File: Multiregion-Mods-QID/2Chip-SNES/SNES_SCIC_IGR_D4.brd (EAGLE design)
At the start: 88.9 x 37.5 mm, 27 parts, among them IC1 74HC27D, IC2 74HC30D

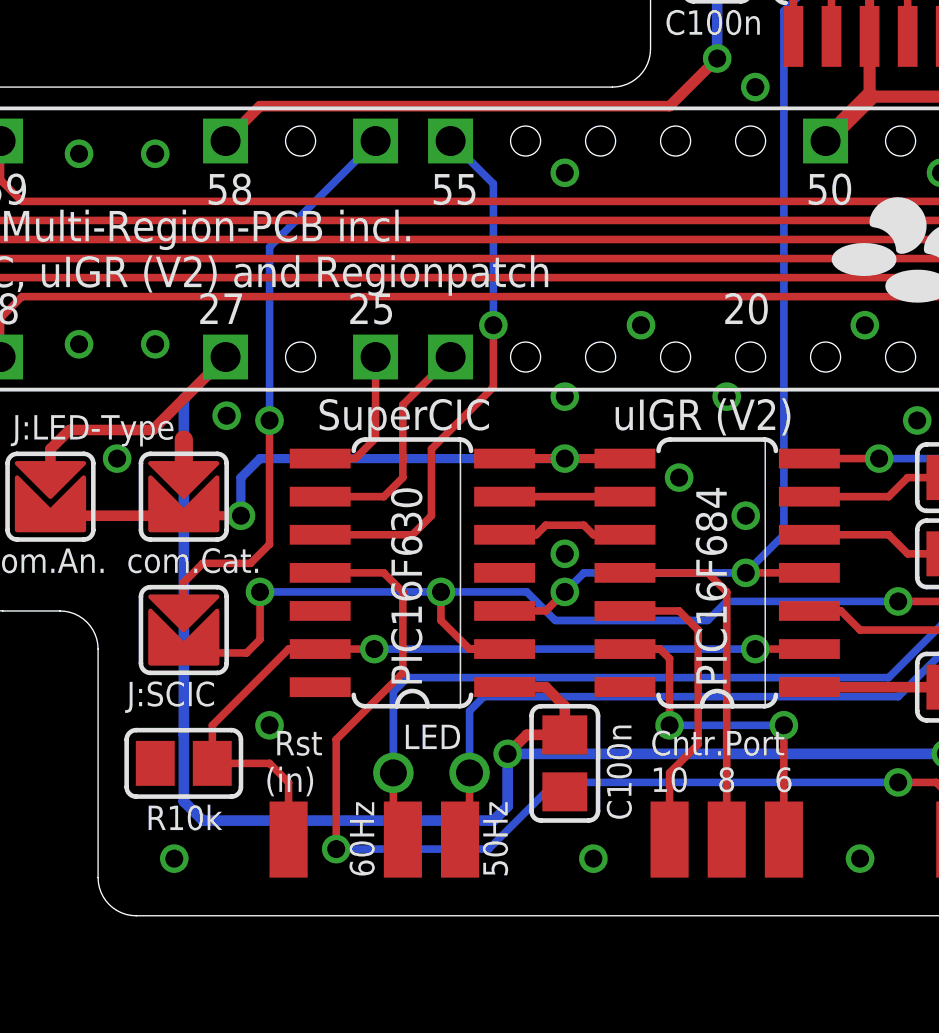
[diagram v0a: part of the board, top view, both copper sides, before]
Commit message: Minor Update (routing of wires from SuperCIC to cart.slot)
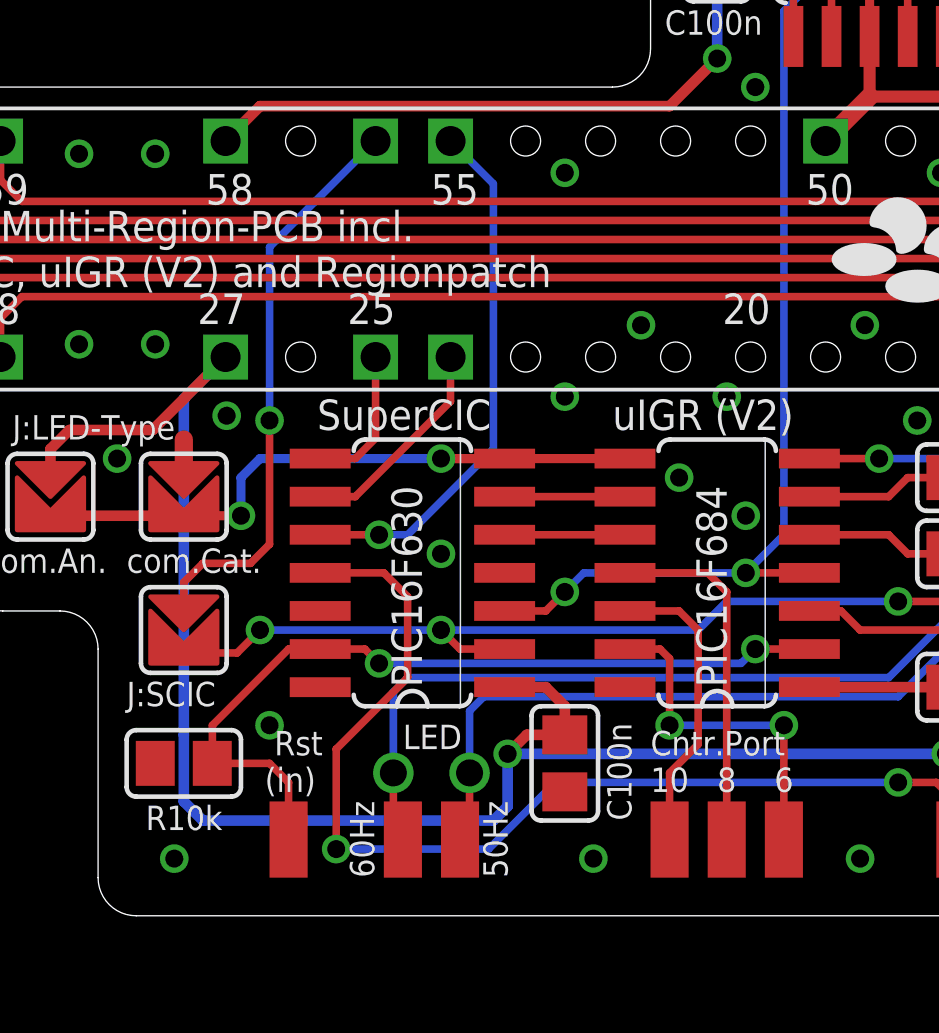
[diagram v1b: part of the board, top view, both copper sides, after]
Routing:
- net N$39: track 39.4 -> 36.6 mm
- net N$49: track 7.70 -> 7.14 mm
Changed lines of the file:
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@@
 <?xml version="1.0" encoding="utf-8"?>
 <!DOCTYPE eagle SYSTEM "eagle.dtd">
-<eagle version="6.4">
+<eagle version="7.2.0">
 <drawing>
 <settings>
@@
 <pass name="Default">
 <param name="RoutingGrid" value="50mil"/>
+<param name="AutoGrid" value="1"/>
+<param name="Efforts" value="0"/>
+<param name="TopRouterVariant" value="1"/>
 <param name="tpViaShape" value="round"/>
 <param name="PrefDir.1" value="|"/>
@@
 <signal name="GND">
 <contactref element="C1" pad="2"/>
-<via x="29.5275" y="17.78" extent="1-16" drill="0.6"/>
+<via x="25.4" y="17.78" extent="1-16" drill="0.6"/>
 <via x="79.375" y="28.575" extent="1-16" drill="0.6"/>
 <via x="74.295" y="28.575" extent="1-16" drill="0.6"/>
@@
 <contactref element="CTRL1" pad="1"/>
 <contactref element="U$1" pad="P$2"/>
-<wire x1="27.5209" y1="14.605" x2="26.3525" y2="14.605" width="0.254" layer="1"/>
-<wire x1="26.3525" y1="14.605" x2="25.4" y2="15.5575" width="0.254" layer="1"/>
-<via x="25.4" y="16.51" extent="1-16" drill="0.6"/>
-<wire x1="25.4" y1="16.51" x2="19.3675" y2="16.51" width="0.254" layer="16"/>
-<wire x1="16.8275" y1="14.474825" x2="18.919825" y2="14.474825" width="0.254" layer="1"/>
-<wire x1="18.919825" y1="14.474825" x2="19.3675" y2="14.9225" width="0.254" layer="1"/>
-<wire x1="19.3675" y1="14.9225" x2="19.3675" y2="16.51" width="0.254" layer="1"/>
-<via x="19.3675" y="16.51" extent="1-16" drill="0.6"/>
-<wire x1="25.4" y1="16.51" x2="28.2575" y2="16.51" width="0.254" layer="16"/>
-<wire x1="28.2575" y1="16.51" x2="29.21" y2="15.5575" width="0.254" layer="16"/>
-<wire x1="29.21" y1="15.5575" x2="34.29" y2="15.5575" width="0.254" layer="16"/>
-<wire x1="34.29" y1="15.5575" x2="34.925" y2="16.1925" width="0.254" layer="16"/>
+<wire x1="27.5209" y1="14.605" x2="26.035" y2="14.605" width="0.254" layer="1"/>
+<via x="25.4" y="15.24" extent="1-16" drill="0.6"/>
+<wire x1="25.4" y1="15.24" x2="19.3675" y2="15.24" width="0.254" layer="16"/>
+<wire x1="16.8275" y1="14.474825" x2="18.602325" y2="14.474825" width="0.254" layer="1"/>
+<wire x1="18.602325" y1="14.474825" x2="19.3675" y2="15.24" width="0.254" layer="1"/>
+<via x="19.3675" y="15.24" extent="1-16" drill="0.6"/>
+<wire x1="25.4" y1="15.24" x2="33.9725" y2="15.24" width="0.254" layer="16"/>
+<wire x1="33.9725" y1="15.24" x2="34.925" y2="16.1925" width="0.254" layer="16"/>
 <wire x1="34.925" y1="16.1925" x2="40.64" y2="16.1925" width="0.254" layer="16"/>
 <via x="40.64" y="16.1925" extent="1-16" drill="0.6"/>
 <wire x1="40.64" y1="16.1925" x2="49.8475" y2="16.1925" width="0.254" layer="1"/>
-<wire x1="25.4" y1="15.5575" x2="25.4" y2="16.51" width="0.254" layer="1"/>
 <wire x1="49.8475" y1="16.1925" x2="50.165" y2="15.875" width="0.254" layer="1"/>
+<wire x1="26.035" y1="14.605" x2="25.4" y2="15.24" width="0.254" layer="1"/>
 </signal>
 <signal name="N$48">
 <contactref element="U$2" pad="10"/>
-<wire x1="21.3741" y1="18.415" x2="24.4475" y2="18.415" width="0.254" layer="1"/>
-<wire x1="24.4475" y1="18.415" x2="25.0825" y2="19.05" width="0.254" layer="1"/>
 <contactref element="U$6" pad="55"/>
-<wire x1="25.0825" y1="19.05" x2="25.0825" y2="21.2725" width="0.254" layer="1"/>
-<via x="27.14625" y="25.4" extent="1-16" drill="0.6"/>
-<wire x1="27.14625" y1="25.4" x2="27.14625" y2="30.11375" width="0.254" layer="16"/>
+<wire x1="27.14625" y1="21.2725" x2="27.14625" y2="30.11375" width="0.254" layer="16"/>
 <wire x1="27.14625" y1="30.11375" x2="25.72" y2="31.54" width="0.254" layer="16"/>
-<wire x1="25.0825" y1="21.2725" x2="27.14625" y2="23.33625" width="0.254" layer="1"/>
-<wire x1="27.14625" y1="23.33625" x2="27.14625" y2="25.4" width="0.254" layer="1"/>
+<wire x1="21.3741" y1="18.415" x2="23.33625" y2="18.415" width="0.254" layer="1"/>
+<via x="23.33625" y="18.415" extent="1-16" drill="0.6"/>
+<wire x1="23.33625" y1="18.415" x2="24.28875" y2="18.415" width="0.254" layer="16"/>
+<wire x1="24.28875" y1="18.415" x2="27.14625" y2="21.2725" width="0.254" layer="16"/>
 </signal>
 <signal name="N$49">
 <contactref element="U$2" pad="9"/>
-<wire x1="21.3741" y1="19.685" x2="23.495" y2="19.685" width="0.254" layer="1"/>
-<wire x1="23.495" y1="19.685" x2="24.13" y2="20.32" width="0.254" layer="1"/>
-<wire x1="24.13" y1="20.32" x2="24.13" y2="22.75" width="0.254" layer="1"/>
-<wire x1="24.13" y1="22.75" x2="25.72" y2="24.34" width="0.254" layer="1"/>
 <contactref element="U$6" pad="24"/>
+<wire x1="21.3741" y1="19.685" x2="22.5425" y2="19.685" width="0.254" layer="1"/>
+<wire x1="22.5425" y1="19.685" x2="25.7175" y2="22.86" width="0.254" layer="1"/>
+<wire x1="25.7175" y1="22.86" x2="25.7175" y2="24.3375" width="0.254" layer="1"/>
+<wire x1="25.7175" y1="24.3375" x2="25.72" y2="24.34" width="0.254" layer="1"/>
 </signal>
 <signal name="N$51">
@@
 <contactref element="RES-OUT" pad="1"/>
 <wire x1="21.3741" y1="17.145" x2="23.495" y2="17.145" width="0.254" layer="1"/>
-<wire x1="23.495" y1="17.145" x2="24.13" y2="16.51" width="0.254" layer="1"/>
-<wire x1="24.13" y1="16.51" x2="24.13" y2="13.81125" width="0.254" layer="1"/>
-<wire x1="24.13" y1="13.81125" x2="21.9075" y2="11.58875" width="0.254" layer="1"/>
-<wire x1="21.9075" y1="11.58875" x2="21.9075" y2="7.9375" width="0.254" layer="1"/>
+<wire x1="23.495" y1="17.145" x2="24.28875" y2="16.35125" width="0.254" layer="1"/>
+<wire x1="24.28875" y1="16.35125" x2="24.28875" y2="13.6525" width="0.254" layer="1"/>
+<wire x1="24.28875" y1="13.6525" x2="21.9075" y2="11.27125" width="0.254" layer="1"/>
+<wire x1="21.9075" y1="11.27125" x2="21.9075" y2="7.9375" width="0.254" layer="1"/>
 <via x="21.9075" y="7.9375" extent="1-16" drill="0.6"/>
 <via x="40.64" y="10.16" extent="1-16" drill="0.6"/>
@@
 <contactref element="R1" pad="2"/>
 <contactref element="RES-IN" pad="1"/>
-<via x="23.1775" y="14.605" extent="1-16" drill="0.6"/>
-<wire x1="23.1775" y1="14.605" x2="35.8775" y2="14.605" width="0.254" layer="16"/>
+<via x="23.33625" y="14.12875" extent="1-16" drill="0.6"/>
 <via x="35.8775" y="14.605" extent="1-16" drill="0.6"/>
 <wire x1="21.3741" y1="14.605" x2="20.32" y2="14.605" width="0.254" layer="1"/>
@@
 <wire x1="19.685" y1="10.795" x2="20.32" y2="10.16" width="0.254" layer="1"/>
 <wire x1="20.32" y1="10.16" x2="20.32" y2="8.255" width="0.254" layer="1"/>
-<wire x1="21.3741" y1="14.605" x2="23.1775" y2="14.605" width="0.254" layer="1"/>
 <wire x1="35.8775" y1="14.605" x2="37.6809" y2="14.605" width="0.254" layer="1"/>
+<wire x1="23.33625" y1="14.12875" x2="35.40125" y2="14.12875" width="0.254" layer="16"/>
+<wire x1="35.40125" y1="14.12875" x2="35.8775" y2="14.605" width="0.254" layer="16"/>
+<wire x1="21.3741" y1="14.605" x2="22.86" y2="14.605" width="0.254" layer="1"/>
+<wire x1="22.86" y1="14.605" x2="23.33625" y2="14.12875" width="0.254" layer="1"/>
 </signal>
 <signal name="N$12">
@@
 <contactref element="U$3" pad="10"/>
 <contactref element="U$2" pad="5"/>
-<wire x1="27.5209" y1="18.415" x2="28.575" y2="18.415" width="0.254" layer="1"/>
-<wire x1="28.575" y1="18.415" x2="28.8925" y2="18.7325" width="0.254" layer="1"/>
-<wire x1="28.8925" y1="18.7325" x2="30.1625" y2="18.7325" width="0.254" layer="1"/>
-<wire x1="30.1625" y1="18.7325" x2="30.48" y2="18.415" width="0.254" layer="1"/>
-<wire x1="30.48" y1="18.415" x2="31.5341" y2="18.415" width="0.254" layer="1"/>
+<wire x1="27.5209" y1="18.415" x2="31.5341" y2="18.415" width="0.254" layer="1"/>
 </signal>
 <signal name="N$52">
@@
 <contactref element="U$2" pad="7"/>
 <contactref element="U$4" pad="P$2"/>
-<wire x1="27.5209" y1="20.955" x2="29.5275" y2="20.955" width="0.3048" layer="1"/>
-<wire x1="29.5275" y1="20.955" x2="31.5341" y2="20.955" width="0.3048" layer="1"/>
-<via x="29.5275" y="20.955" extent="1-16" drill="0.6"/>
+<wire x1="27.5209" y1="20.955" x2="25.4" y2="20.955" width="0.3048" layer="1"/>
+<wire x1="25.4" y1="20.955" x2="31.5341" y2="20.955" width="0.3048" layer="1"/>
+<via x="25.4" y="20.955" extent="1-16" drill="0.6"/>
 <contactref element="U$5" pad="P$2"/>
-<wire x1="19.3675" y1="20.955" x2="29.5275" y2="20.955" width="0.3048" layer="16"/>
+<wire x1="19.3675" y1="20.955" x2="25.4" y2="20.955" width="0.3048" layer="16"/>
 <wire x1="19.3675" y1="20.955" x2="18.7325" y2="20.32" width="0.3048" layer="16"/>
 <wire x1="16.8275" y1="18.919825" x2="17.014825" y2="18.919825" width="0.3048" layer="1"/>
